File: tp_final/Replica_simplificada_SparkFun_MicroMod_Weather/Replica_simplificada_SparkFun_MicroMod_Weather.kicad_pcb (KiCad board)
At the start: 2 copper layers, 38.7 x 40 mm, 32 parts, among them J1 USB_C_Receptacle_USB2.0, J2 Conn_01x05, J3 Conn_01x02, J4 Conn_01x03, U1 BME280, U2 AP7361C-33F, U3 AS3935

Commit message: Primeras correciones
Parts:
- added REF**: Fiducial_0.5mm_Mask1.5mm, Fiducial:Fiducial_0.5mm_Mask1.5mm, F.Cu at (156.5, 83.3)
- added REF**: Fiducial_0.5mm_Mask1.5mm, Fiducial:Fiducial_0.5mm_Mask1.5mm, F.Cu at (130.6, 83.3)
- added REF**: Fiducial_0.5mm_Mask1.5mm, Fiducial:Fiducial_0.5mm_Mask1.5mm, F.Cu at (130.6, 116.3)
- added REF**: Fiducial_0.5mm_Mask1.5mm, Fiducial:Fiducial_0.5mm_Mask1.5mm, F.Cu at (157.0, 116.8)
- added REF**: MountingHole_2.2mm_M2_ISO7380, MountingHole:MountingHole_2.2mm_M2_ISO7380, F.Cu at (160.5, 116.8)
- added REF**: MountingHole_2.2mm_M2_ISO7380, MountingHole:MountingHole_2.2mm_M2_ISO7380, F.Cu at (127.0, 116.3)
- added REF**: MountingHole_2.2mm_M2_ISO7380, MountingHole:MountingHole_2.2mm_M2_ISO7380, F.Cu at (127.0, 83.3)
- added REF**: MountingHole_2.2mm_M2_ISO7380, MountingHole:MountingHole_2.2mm_M2_ISO7380, F.Cu at (160.0, 83.3)
- moved D2 17.7 mm to (140.5, 100.1)
- moved R6 16.9 mm to (144.4, 100.1)
- moved R1 9.18 mm to (154.4, 115.8)
- moved C5 9.16 mm to (150.4, 115.8)
- moved J1 5.68 mm to (159.4, 106.0)
- moved J2 5.64 mm to (128.0, 88.4)
- moved C10 5.61 mm to (136.7, 94.7)
- moved C11 5.61 mm to (140.5, 94.7)
- moved R8 4.34 mm to (150.9, 110.9)
- moved R9 4.34 mm to (150.9, 107.8)
- moved D1 3.70 mm to (134.4, 115.3)
- moved D3 3.31 mm to (136.7, 100.1)
- moved R7 3.06 mm to (131.6, 102.6), turned to 0 degrees
- moved R4 2.96 mm to (148.8, 94.0)
- moved C2 2.87 mm to (147.8, 83.3)
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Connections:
- J4 pad 1: I2C_SDA -> I2C_SCK
- J4 pad 2: I2C_SCK -> I2C_SDA
- U1 pad 3: I2C_SCK -> I2C_SDA
- U1 pad 4: I2C_SDA -> I2C_SCK
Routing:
- net GND: track 112.7 -> 119.8 mm, vias 8 -> 6
- net +3V3: track 9.25 -> 3.57 mm
- net +5V: track 38.9 -> 43.7 mm
- net /SPI_~CS~: track 25.7 -> 30.1 mm
- net Net-(D3-Pad2): track 3.84 -> 6.70 mm
- net I2C_SCK: track 10.6 -> 8.15 mm
- net /SPI_MISO: track 7.01 -> 9.41 mm
- net /SPI_MOSI: track 8.66 -> 11.1 mm
- net I2C_SDA: track 8.53 -> 10.0 mm
- net /SPI_SCK: track 7.55 -> 8.62 mm
- net 3.3V_EN: track 5.71 -> 4.69 mm
- net Net-(C6-Pad1): track 14.0 -> 13.0 mm
- net Net-(D2-Pad2): track 3.19 -> 3.95 mm
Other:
- board size 38.7 x 40 mm -> 40.1 x 40.1 mm
- board text added: "+"
- board text added: "Ind. Argentina v1"
- board text added: "LIGHT."
- board text added: "Margen: 6 mils Grilla: 20 mils"
- board text added: "Minimo ancho de pista: 5 mils Minimo diamtero via: 1.1 mm Minimo taladro: 0.5 mm"
- board text added: "Replica SparkFun MicroMod Weather"
- board text added: "Valores tomados en base a fabricante: Mayer PCB"
- board text removed: "LIGHTING"

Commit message: Mejoro posicionamiento
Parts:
- moved R9 3.07 mm to (148.5, 109.7), turned to 270 degrees
- moved U1 2.09 mm to (151.9, 97.9)
- moved R7 1.44 mm to (132.6, 101.6), turned to 90 degrees
- moved R8 1.31 mm to (151.5, 109.7), turned to 270 degrees
- moved R4 1.02 mm to (148.3, 94.9), turned to 270 degrees
- moved JP1 0.36 mm to (138.2, 115.6), turned to 270 degrees
- turned C2 to 270 degrees
- turned C8 to 270 degrees
- turned R5 to 270 degrees
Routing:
- net GND: track 119.8 -> 127.7 mm
- net Net-(J1-PadB5): track 5.44 -> 8.90 mm
- net I2C_SCK: track 8.15 -> 5.91 mm
- net Net-(D3-Pad2): track 6.70 -> 4.67 mm
- net I2C_SDA: track 10.0 -> 8.26 mm
- net /SPI_~CS~: track 30.1 -> 28.9 mm
- net Net-(J1-PadA5): track 5.43 -> 4.61 mm
- net Net-(D1-Pad1): track 10.9 -> 11.7 mm
- net Net-(R4-Pad2): track 3.74 -> 4.36 mm
- net 3.3V_EN: track 4.69 -> 5.27 mm
- net Net-(R3-Pad2): track 3.01 -> 3.56 mm

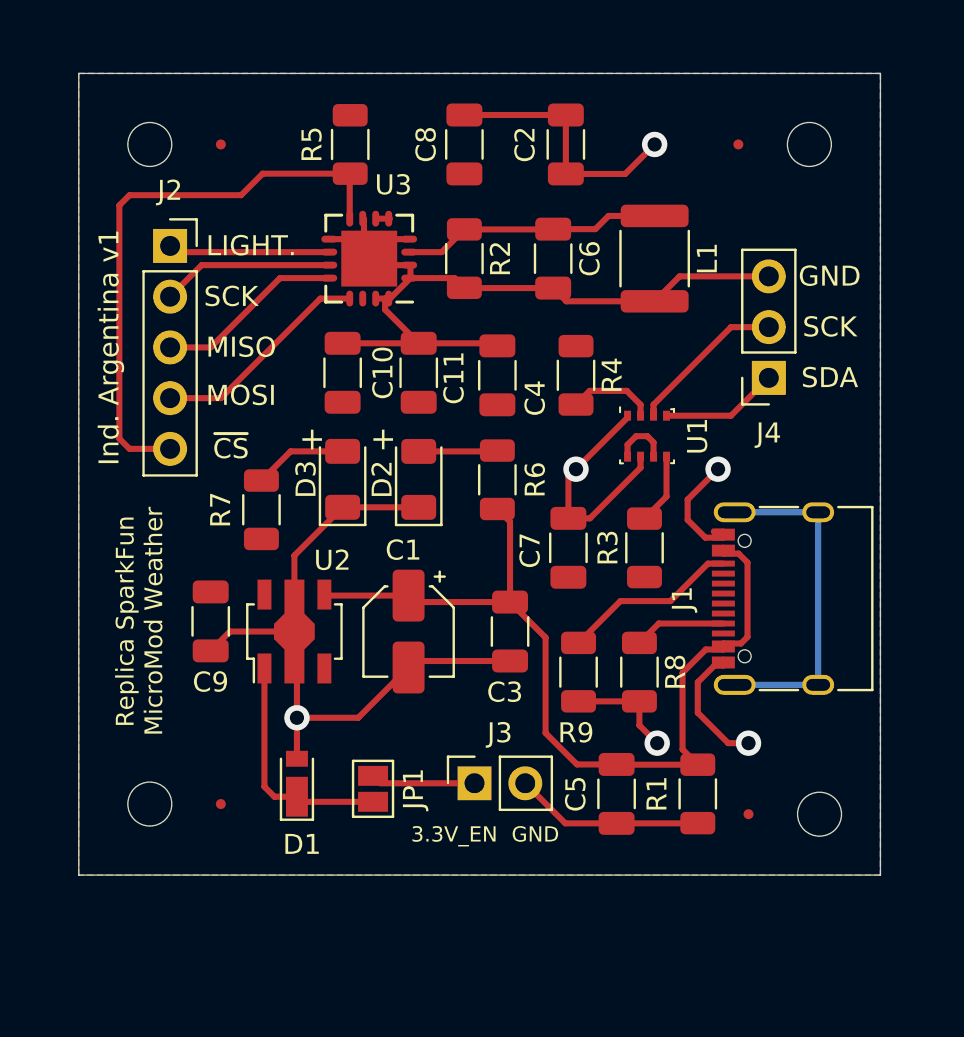
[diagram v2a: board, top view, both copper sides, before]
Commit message: Agrego mounting hole y fiduciales al esquematico
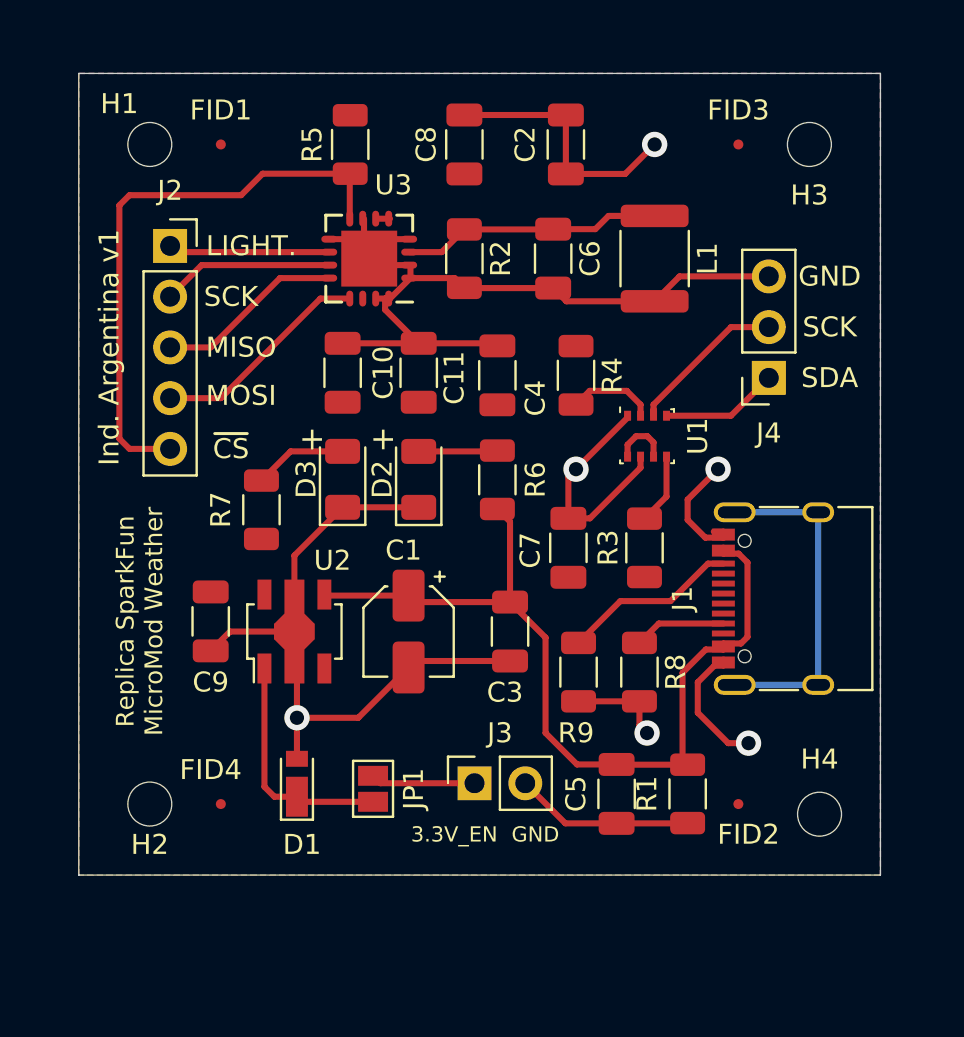
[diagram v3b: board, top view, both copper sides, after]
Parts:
- removed REF** (x4): Fiducial_0.5mm_Mask1.5mm, Fiducial:Fiducial_0.5mm_Mask1.5mm
- removed REF** (x4): MountingHole_2.2mm_M2_ISO7380, MountingHole:MountingHole_2.2mm_M2_ISO7380
- added FID1: Fiducial, Fiducial:Fiducial_0.5mm_Mask1.5mm, F.Cu at (130.6, 83.3)
- added FID2: Fiducial, Fiducial:Fiducial_0.5mm_Mask1.5mm, F.Cu at (156.5, 116.3)
- added FID3: Fiducial, Fiducial:Fiducial_0.5mm_Mask1.5mm, F.Cu at (156.5, 83.3)
- added FID4: Fiducial, Fiducial:Fiducial_0.5mm_Mask1.5mm, F.Cu at (130.6, 116.3)
- added H1: MountingHole, MountingHole:MountingHole_2.2mm_M2_ISO7380, F.Cu at (127.0, 83.3)
- added H2: MountingHole, MountingHole:MountingHole_2.2mm_M2_ISO7380, F.Cu at (127.0, 116.3)
- added H3: MountingHole, MountingHole:MountingHole_2.2mm_M2_ISO7380, F.Cu at (160.0, 83.3)
- added H4: MountingHole, MountingHole:MountingHole_2.2mm_M2_ISO7380, F.Cu at (160.5, 116.8)
- moved R1 0.51 mm to (153.9, 115.8)
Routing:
- net GND: track 127.7 -> 127.0 mm

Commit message: Correciones finales
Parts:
- removed C2: 10u, Capacitor_SMD:C_1206_3216Metric
- C1, C9: value 10u -> 10uF
- C10, C8: value 1u -> 1uF
- C11, C3: value 0.22u -> 0.22uF
- C4, C7: value 0.1u -> 0.1uF
- C6: value 1n -> 1nC
- L1: value 100u -> 100uH
- moved C4 15.0 mm to (157.0, 103.0), turned to 0 degrees
- moved C9 11.3 mm to (141.0, 104.5), turned to 90 degrees
- moved C10 10.4 mm to (133.0, 104.5)
- moved C11 10.4 mm to (137.0, 104.5)
- moved R7 5.56 mm to (137.5, 99.0)
- moved C3 5.30 mm to (145.0, 113.0)
- moved D3 4.97 mm to (141.5, 99.0)
- moved FID4 4.70 mm to (130.0, 121.0)
- moved FID2 4.70 mm to (157.0, 121.0)
- moved H2 4.69 mm to (126.5, 121.0)
- moved D2 4.66 mm to (145.0, 99.0), turned to 270 degrees
- moved C8 4.54 mm to (144.5, 87.5)
- moved R6 4.44 mm to (145.0, 104.5)
- moved R5 4.19 mm to (137.0, 87.5)
- moved H4 4.16 mm to (160.5, 121.0)
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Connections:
- net 3.3V_EN renamed /3.3V_EN
- net I2C_SCK renamed /I2C_SCK
- net I2C_SDA renamed /I2C_SDA
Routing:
- net GND: track 127.0 -> 86.6 mm, vias 6 -> 24
- net +5V: track 43.5 -> 63.2 mm
- net Net-(D2-Pad2): track 3.95 -> 2.64 mm
- net +3V3: track 3.57 -> 4.57 mm
- net Net-(R3-Pad2): track 3.56 -> 4.54 mm
- net /I2C_SCK: track 5.91 -> 5.12 mm
- net /3.3V_EN: track 5.27 -> 4.52 mm
- net /SPI_~CS~: track 28.9 -> 28.3 mm
- net Net-(D3-Pad2): track 4.67 -> 4.03 mm
- net /I2C_SDA: track 8.26 -> 8.80 mm
- net /LIGHTING_IRQ: track 8.10 -> 8.62 mm
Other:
- board size 40.1 x 40.1 mm -> 40 x 40 mm
- net class Default: clearance 0.1524 -> 0.2; trace_width 0.3048 -> 0.3; via_drill 0.7112 -> 0.7
- rule trace_clearance: 0.1524 -> 0.2
- rule trace_min: 0.127 -> 0.3
- rule via_min_drill: 0.5 -> 0.7
- rule via_min_size: 1.1096 -> 1.27
- board text added: "I2C TEMP HUMEDAD,PRESION"
- board text added: "Industria Argentina v1"
- board text added: "Minimos en base a fabricante Mayer PCB (12 mils) Margen: 1mm Grillas: 1mm, 0.5mm Minimo ancho de pista: 0.3mm Diametro de via: 1.27 mm Diametro de agujero: 0.7 mm Terminación: HASL"
- board text added: "SPI Detector de rayos"
- board text added: "Simplificación SparkFun MicroMod Weather"
- board text removed: "Ind. Argentina v1"
- board text removed: "Margen: 6 mils Grilla: 20 mils"
- board text removed: "Minimo ancho de pista: 5 mils Minimo diamtero via: 1.1 mm Minimo taladro: 0.5 mm"
- board text removed: "Replica SparkFun MicroMod Weather"
- board text removed: "Valores tomados en base a fabricante: Mayer PCB"
